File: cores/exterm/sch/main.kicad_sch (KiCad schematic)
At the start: 27 parts

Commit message: almost ready
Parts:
- R1: renamed from R1KΩ; value R1 -> R1KΩ
- R19: renamed from R330Ω; value R19 -> R330Ω
- R2: renamed from R330Ω; value R2 -> R330Ω
- R20: renamed from R330Ω; value R20 -> R330Ω
- R31: renamed from R1KΩ; value R31 -> R1KΩ
- RR15: renamed from R150Ω; value R5 -> R150Ω
- renumbered C4 to CC4
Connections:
- net PULL DOWN: now also RR15.2; no longer RR15.1
- net VCC: now also R20.2; no longer R20.1
- net XTAL1: now also R20.1; no longer R20.2
- net at B13.3 (A1), CC4.1: now also RR15.1; no longer RR15.2
- net DVAL renamed SPBANK1
- net MAIN_WR renamed ~{WR}
- net MAIN_~{INT}: no longer names the net of B4.6 (~{Q}), E8.16 (~{INT})
- net QB renamed QH
- net R_A14: no longer names the net of C9.27 (A14)
- no-connect marks 15 -> 16
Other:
- note added: "DRIVER"
- note removed: "?"
- moved on the sheet: B4A, R19, R2

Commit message: exterm_kiwi
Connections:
- net VCC: no longer D6.20 (VCC)
- net VSS: no longer D6.10 (GND)
- net BANK_CFG0: now reaches C9.27 (A14)
- net BANK_CFG0: now also B5.2 (Q0), D6.6 (I6)
- net AQUI: no longer names the net of D6.19 (IO1)
- net CFG0 renamed GFX_A11
- net GFX_A11: no longer B5.2 (Q0)
- net CFG1 renamed BANK_CFG1
- net BANK_CFG1: no longer D6.6 (I6)
- net CFG2 renamed BANK_CFG2
- net CFG4 renamed ~{SND_RST'}
- net MAIN_AD renamed ~{BANK_CFG1}
- net SND_SELECT renamed ~{SND_SELECT} 
- net ~{CFG1} renamed ~{BANK_CFG0}
- net ~{RESET} renamed ~{SND_RST}
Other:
- moved on the sheet: B2A, B2C, C3, D6

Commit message: issues_exterm
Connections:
- net VCC: now also D6.20 (VCC)
- net VSS: now also D6.10 (GND)
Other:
- note added: "DRIVER?"
- note removed: "DRIVER"
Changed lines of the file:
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@@
     (stroke (width 0) (type default) (color 0 0 0 0))
   )
-  (wire (pts (xy 374.015 25.4) (xy 374.015 27.94))
+  (wire (pts (xy 374.65 25.4) (xy 374.65 27.94))
     (stroke (width 0) (type default) (color 0 0 0 0))
   )
@@
     (stroke (width 0) (type default) (color 0 0 0 0))
   )
-  (wire (pts (xy 374.015 60.96) (xy 374.015 64.77))
+  (wire (pts (xy 374.65 60.96) (xy 374.65 64.77))
     (stroke (width 0) (type default) (color 0 0 0 0))
   )
@@
     )
   )
-  (text "DRIVER" (at 147.32 67.31 0)
-    (effects (font (size 1.27 1.27)) (justify left bottom))
-  )
   (text "CPU MAIN\n" (at 165.1 82.55 0)
     (effects (font (size 1.27 1.27)) (justify left bottom))
   )
+  (text "DRIVER?" (at 257.81 205.74 0)
+    (effects (font (size 1.27 1.27)) (justify left bottom))
+  )
   (label "GFX_CLK" (at 78.74 226.06 180)
     (effects (font (size 1.27 1.27)) (justify right bottom))
@@
     (effects (font (size 1.27 1.27)) (justify left bottom))
   )
-  (label "VCC" (at 374.015 25.4 0)
+  (label "VCC" (at 374.65 25.4 0)
     (effects (font (size 1.27 1.27)) (justify left bottom))
   )
@@
     (effects (font (size 1.27 1.27)) (justify left bottom))
   )
-  (label "VSS" (at 374.015 64.77 0)
-    (effects (font (size 1.27 1.27)) (justify left bottom))
-  )
+  (label "VSS" (at 374.65 64.77 0)
+    (effects (font (size 1.27 1.27)) (justify left bottom))
+  )

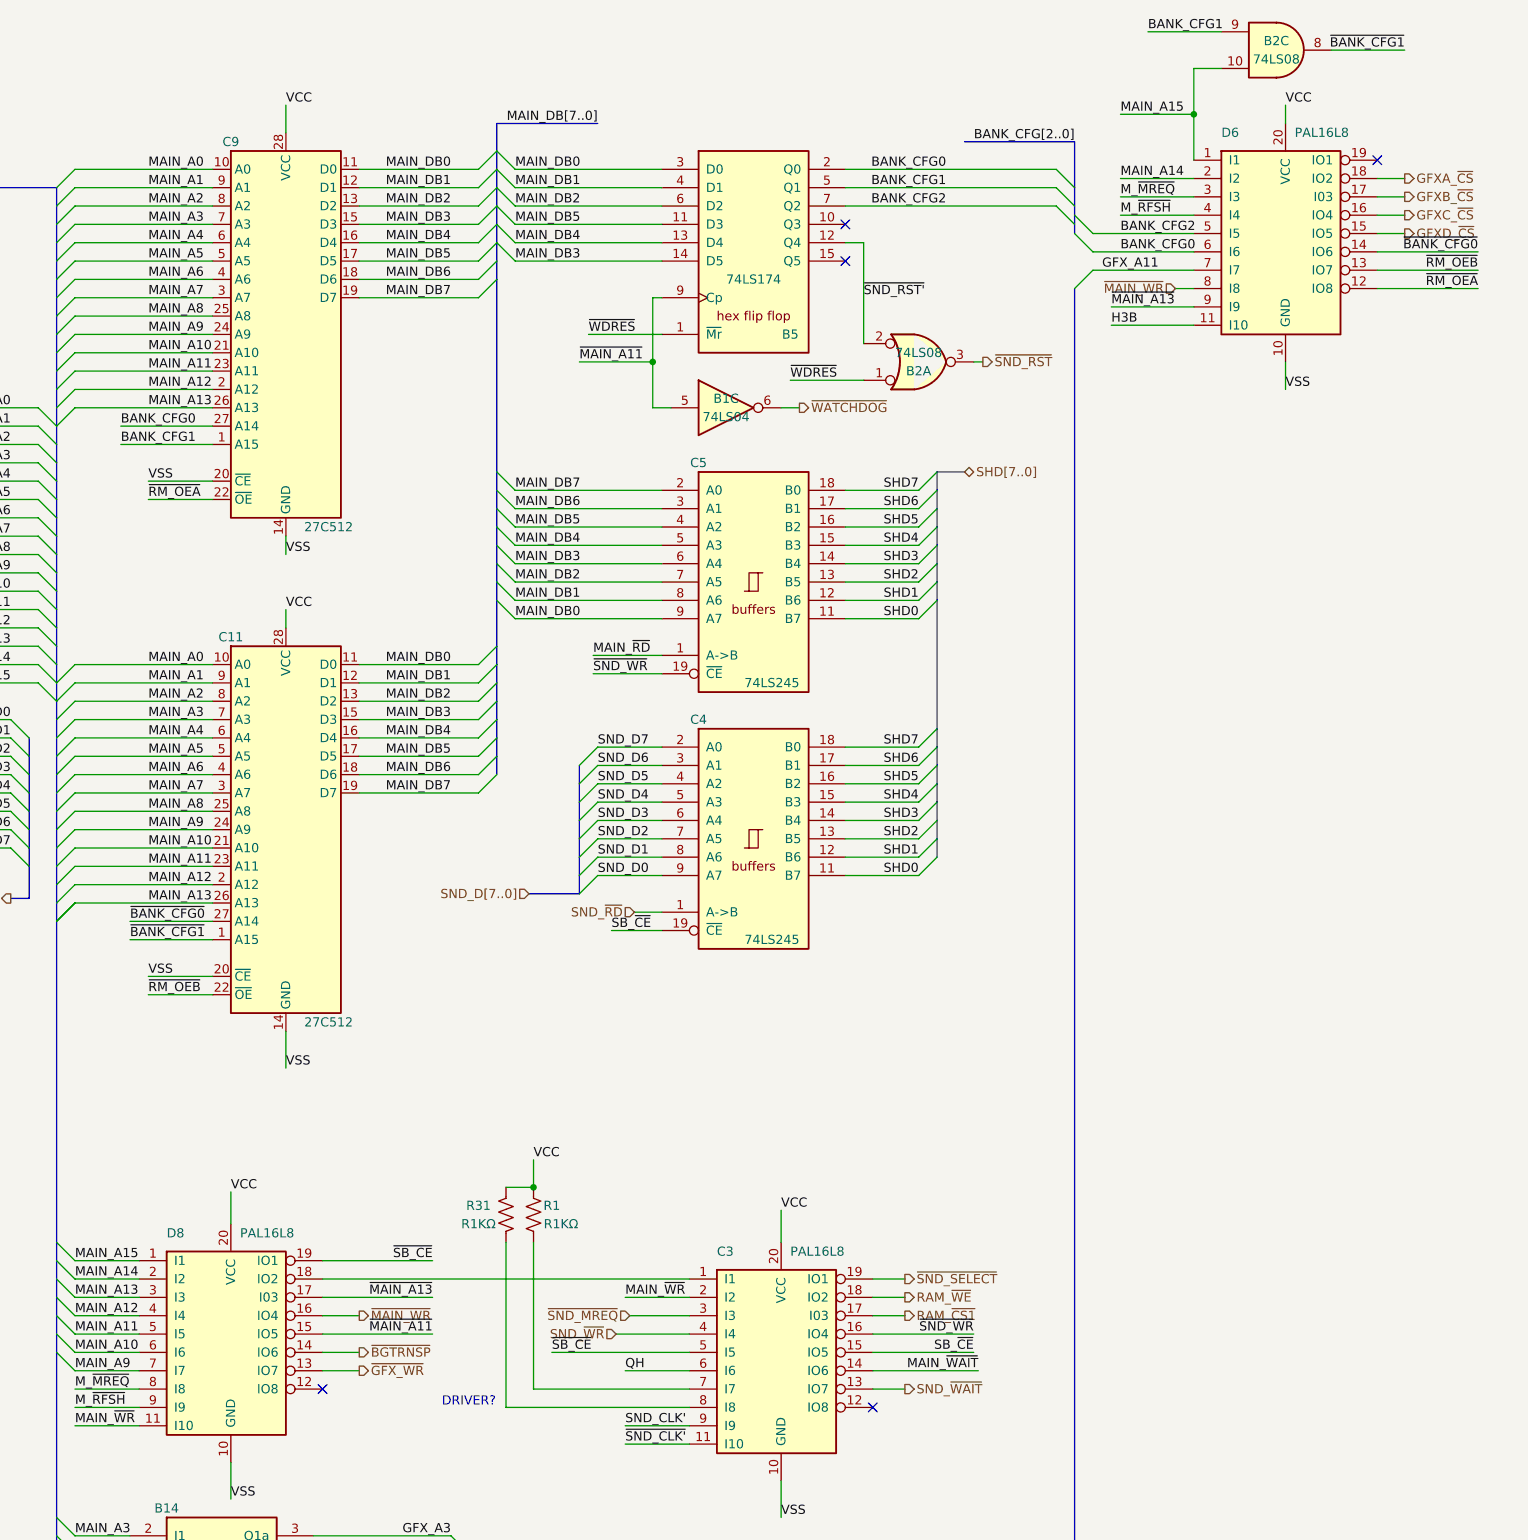
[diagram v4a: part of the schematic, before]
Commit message: changed sym-lib-table to symbolic links
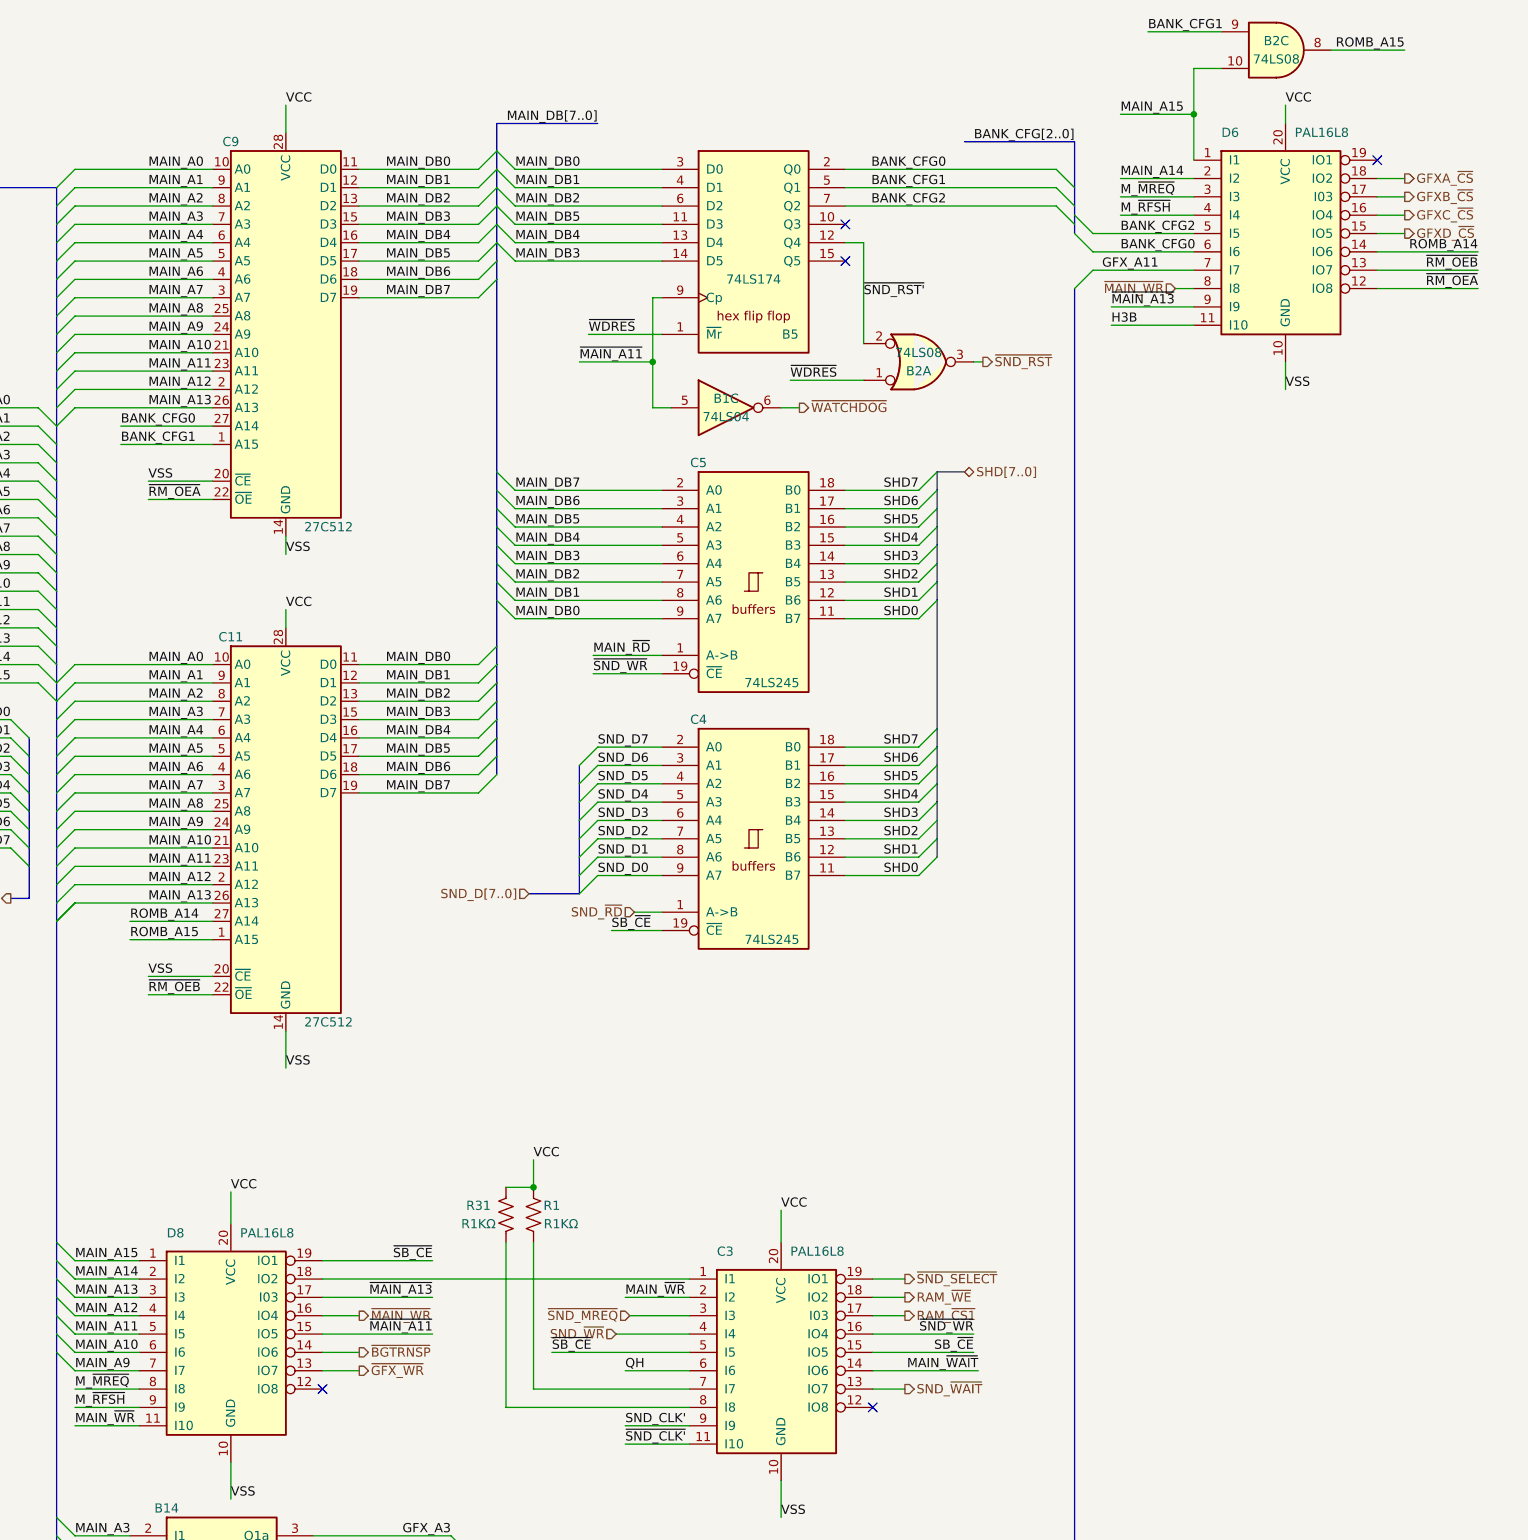
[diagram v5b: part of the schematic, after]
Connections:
- net ~{BANK_CFG0} renamed ROMB_A14
- net ~{BANK_CFG1} renamed ROMB_A15
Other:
- note removed: "DRIVER?"
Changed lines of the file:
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@@
-    (effects (font (size 1.27 1.27)) (justify left bottom))
-  )
-  (text "DRIVER?" (at 257.81 205.74 0)
     (effects (font (size 1.27 1.27)) (justify left bottom))
   )
@@
     (effects (font (size 1.27 1.27)) (justify right bottom))
   )
-  (label "~{BANK_CFG1}" (at 214.63 140.97 0)
+  (label "ROMB_A15" (at 214.63 140.97 0)
     (effects (font (size 1.27 1.27)) (justify left bottom))
   )
@@
     (effects (font (size 1.27 1.27)) (justify left bottom))
   )
-  (label "~{BANK_CFG1}" (at 391.16 17.78 180)
+  (label "ROMB_A15" (at 391.16 17.78 180)
     (effects (font (size 1.27 1.27)) (justify right bottom))
   )
@@
     (effects (font (size 1.27 1.27)) (justify right bottom))
   )
-  (label "~{BANK_CFG0}" (at 401.32 45.72 180)
+  (label "ROMB_A14" (at 401.32 45.72 180)
     (effects (font (size 1.27 1.27)) (justify right bottom))
   )
@@
     (effects (font (size 1.27 1.27)) (justify right bottom))
   )
-  (label "~{BANK_CFG0}" (at 214.63 138.43 0)
-    (effects (font (size 1.27 1.27)) (justify left bottom))
-  )
+  (label "ROMB_A14" (at 214.63 138.43 0)
+    (effects (font (size 1.27 1.27)) (justify left bottom))
+  )

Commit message: issues_solved_#21
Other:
- note removed: "CPU MAIN"
- moved on the sheet: B2C
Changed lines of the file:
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@@
     (stroke (width 0) (type default) (color 0 0 0 0))
   )
-  (wire (pts (xy 361.95 20.32) (xy 361.95 26.67))
+  (wire (pts (xy 361.95 22.86) (xy 361.95 26.67))
     (stroke (width 0) (type default) (color 0 0 0 0))
   )
@@
     (stroke (width 0) (type default) (color 0 0 0 0))
   )
-  (wire (pts (xy 374.65 25.4) (xy 374.65 27.94))
+  (wire (pts (xy 377.19 27.94) (xy 374.65 27.94))
     (stroke (width 0) (type default) (color 0 0 0 0))
   )
@@
     (stroke (width 0) (type default) (color 0 0 0 0))
   )
-  (wire (pts (xy 355.6 15.24) (xy 365.76 15.24))
+  (wire (pts (xy 355.6 17.78) (xy 365.76 17.78))
     (stroke (width 0) (type default) (color 0 0 0 0))
   )
@@
     (stroke (width 0) (type default) (color 0 0 0 0))
   )
-  (wire (pts (xy 52.07 276.225) (xy 52.07 280.67))
+  (wire (pts (xy 52.07 276.225) (xy 52.07 281.94))
     (stroke (width 0) (type default) (color 0 0 0 0))
   )
@@
     (stroke (width 0) (type default) (color 0 0 0 0))
   )
-  (wire (pts (xy 361.95 20.32) (xy 365.76 20.32))
+  (wire (pts (xy 361.95 22.86) (xy 365.76 22.86))
     (stroke (width 0) (type default) (color 0 0 0 0))
   )
@@
     (stroke (width 0) (type default) (color 0 0 0 0))
   )
-  (wire (pts (xy 381 17.78) (xy 391.16 17.78))
+  (wire (pts (xy 381 20.32) (xy 391.16 20.32))
     (stroke (width 0) (type default) (color 0 0 0 0))
   )
@@
     (stroke (width 0) (type default) (color 0 0 0 0))
   )
-  (image (at 398.78 261.62) (scale 0.294008)
+  (image (at 397.51 261.62) (scale 0.294008)
     (data
       iVBORw0KGgoAAAANSUhEUgAAAtEAAAGsCAMAAAAsQwu3AAAAA3NCSVQICAjb4U/gAAADAFBMVEX/
@@
     )
   )
-  (text "CPU MAIN\n" (at 165.1 82.55 0)
-    (effects (font (size 1.27 1.27)) (justify left bottom))
-  )
   (label "GFX_CLK" (at 78.74 226.06 180)
     (effects (font (size 1.27 1.27)) (justify right bottom))
@@
     (effects (font (size 1.27 1.27)) (justify left bottom))
   )
-  (label "BANK_CFG1" (at 355.6 15.24 0)
+  (label "BANK_CFG1" (at 355.6 17.78 0)
     (effects (font (size 1.27 1.27)) (justify left bottom))
   )
@@
     (effects (font (size 1.27 1.27)) (justify left bottom))
   )
-  (label "VCC" (at 374.65 25.4 0)
+  (label "VCC" (at 377.19 27.94 0)
     (effects (font (size 1.27 1.27)) (justify left bottom))
   )
@@
     (effects (font (size 1.27 1.27)) (justify left bottom))
   )
-  (label "ROMB_A15" (at 391.16 17.78 180)
+  (label "ROMB_A15" (at 391.16 20.32 180)
     (effects (font (size 1.27 1.27)) (justify right bottom))
   )
@@
     (effects (font (size 1.27 1.27)) (justify right bottom))
   )
-  (label "VSS" (at 52.07 280.67 0)
+  (label "VSS" (at 52.07 281.94 0)
     (effects (font (size 1.27 1.27)) (justify left bottom))
   )
@@
     (pin "9")
   )
-  (symbol (lib_id "jt74:74LS08") (at 373.38 17.78 0) (unit 3)
+  (symbol (lib_id "jt74:74LS08") (at 373.38 20.32 0) (unit 3)
     (in_bom yes) (on_board yes)
-    (property "Reference" "B2" (id 0) (at 373.38 16.51 0))
-    (property "Value" "74LS08" (id 1) (at 373.38 19.05 0))
-    (property "Footprint" "" (id 2) (at 373.38 17.78 0)
+    (property "Reference" "B2" (id 0) (at 373.38 19.05 0))
+    (property "Value" "74LS08" (id 1) (at 373.38 21.59 0))
+    (property "Footprint" "" (id 2) (at 373.38 20.32 0)
       (effects (font (size 1.27 1.27)) hide)
     )
-    (property "Datasheet" "http://www.ti.com/lit/gpn/sn74LS08" (id 3) (at 373.38 17.78 0)
+    (property "Datasheet" "http://www.ti.com/lit/gpn/sn74LS08" (id 3) (at 373.38 20.32 0)
       (effects (font (size 1.27 1.27)) hide)
     )

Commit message: Extermination schematics updated (issue #33)
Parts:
- removed B14, C14: 74LS367, symbol jt74:74LS367
- removed G13: 74LS04, symbol jt74:74LS04
- removed R20: R330Ω, symbol Device:R_US
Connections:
- net GFX_A11 renamed VA11
- net GFX_CLK renamed H4B
- net MAIN_DB0 renamed MAIN_VD8
- net MAIN_DB1 renamed MAIN_VD9
- net MAIN_DB2 renamed MAIN_VD10
- net MAIN_DB3 renamed MAIN_VD11
- net MAIN_DB4 renamed MAIN_VD12
- net MAIN_DB5 renamed MAIN_VD13
- net MAIN_DB6 renamed MAIN_VD14
- net MAIN_DB7 renamed MAIN_VD15
- net XTAL1 renamed H1B
- no-connect marks 16 -> 15
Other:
- moved on the sheet: B13, B1A, B1C, B2A, B2B, B2C, B3A, B3B, B4A, B4B, B5, B6B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
